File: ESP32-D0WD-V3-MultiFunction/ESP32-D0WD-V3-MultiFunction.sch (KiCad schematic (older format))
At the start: 0 parts

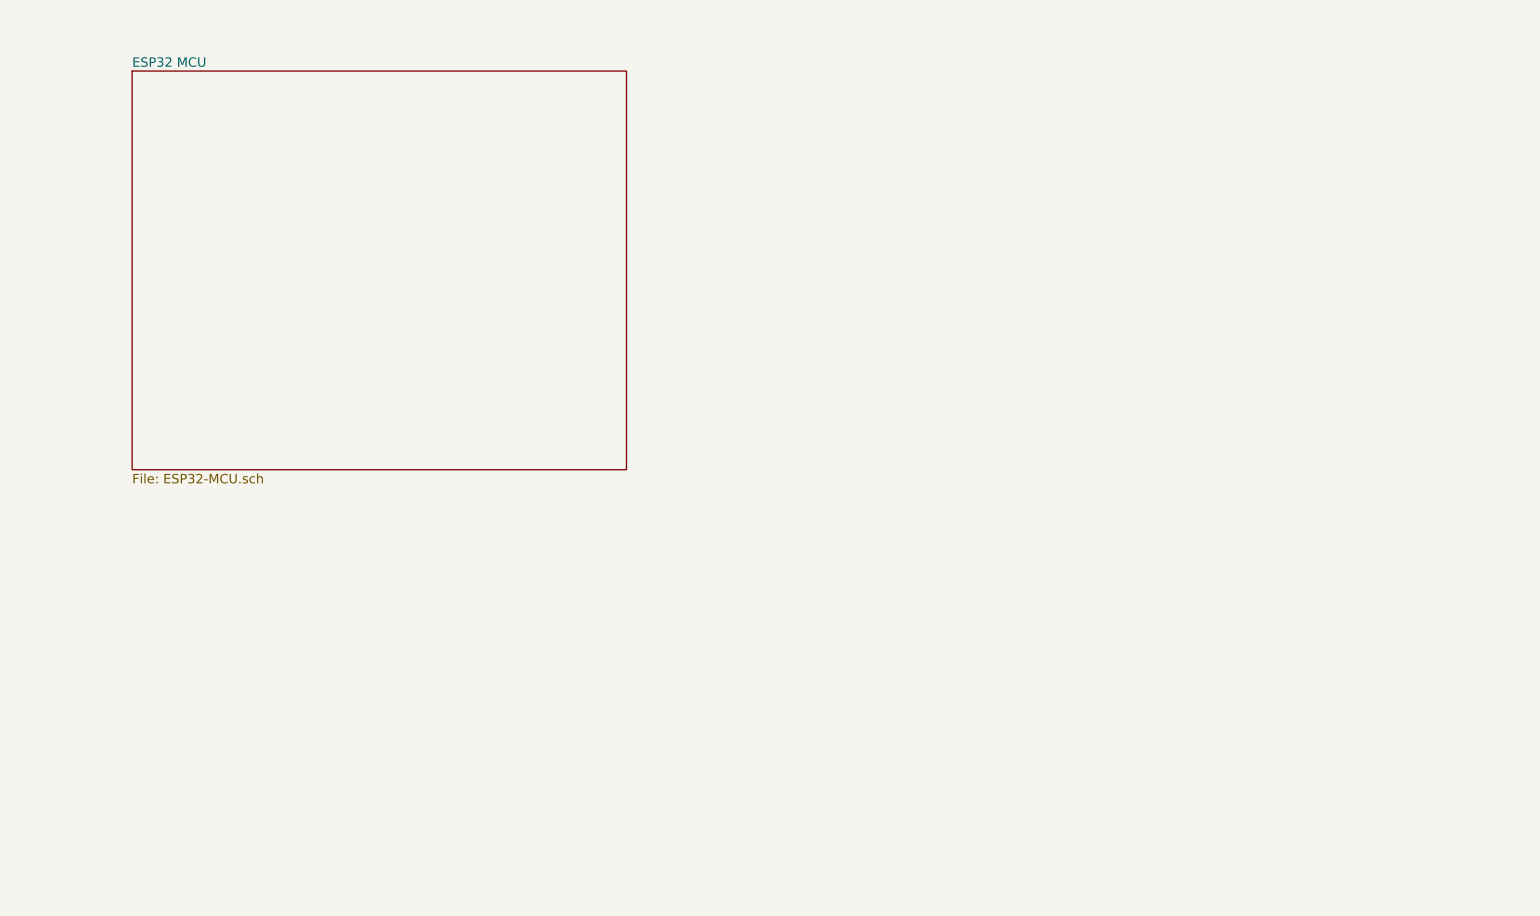
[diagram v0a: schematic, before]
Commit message: Initial draft of bare-chip ESP32 Multifunction board.
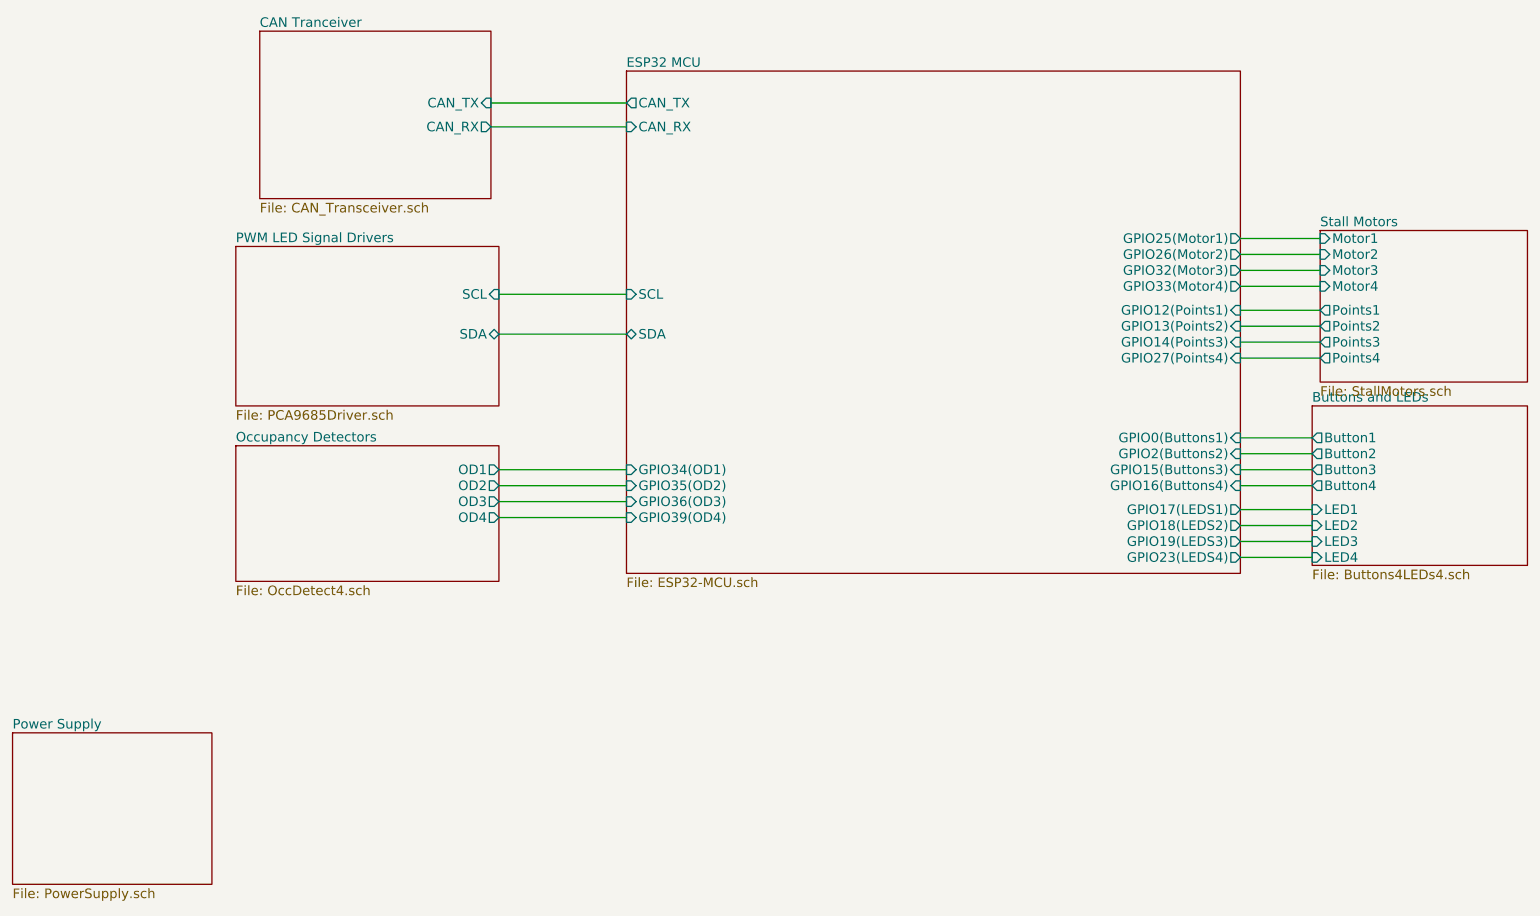
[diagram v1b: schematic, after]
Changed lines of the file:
@@
 LIBS:ESP32-D0WD-V3
 LIBS:W25Q32JVSSIQ
+LIBS:umh3n
+LIBS:lm2574n-5
+LIBS:tc442x
+LIBS:4814p-2
+LIBS:pca9685
+LIBS:tbd62x83a
+LIBS:sn65hvd233-ht
+LIBS:ESP32-D0WD-V3-MultiFunction-cache
 EELAYER 25 0
 EELAYER END
 $Descr A4 11693 8268
 encoding utf-8
-Sheet 1 2
+Sheet 1 8
 Title ""
 Date ""
@@
 $EndDescr
 $Sheet
-S 2050 1350 3100 2500
+S 5150 1350 3850 3150
 U 62ACDEF5
 F0 "ESP32 MCU" 59
 F1 "ESP32-MCU.sch" 59
+F2 "CAN_TX" O L 5150 1550 60
+F3 "CAN_RX" I L 5150 1700 60
+F4 "SCL" I L 5150 2750 60
+F5 "SDA" B L 5150 3000 60
+F6 "GPIO19(LEDS3)" O R 9000 4300 60
+F7 "GPIO23(LEDS4)" O R 9000 4400 60
+F8 "GPIO18(LEDS2)" O R 9000 4200 60
+F9 "GPIO17(LEDS1)" O R 9000 4100 60
+F10 "GPIO16(Buttons4)" I R 9000 3950 60
+F11 "GPIO0(Buttons1)" I R 9000 3650 60
+F12 "GPIO2(Buttons2)" I R 9000 3750 60
+F13 "GPIO27(Points4)" I R 9000 3150 60
+F14 "GPIO26(Motor2)" O R 9000 2500 60
+F15 "GPIO25(Motor1)" O R 9000 2400 60
+F16 "GPIO34(OD1)" I L 5150 3850 60
+F17 "GPIO35(OD2)" I L 5150 3950 60
+F18 "GPIO36(OD3)" I L 5150 4050 60
+F19 "GPIO39(OD4)" I L 5150 4150 60
+F20 "GPIO32(Motor3)" O R 9000 2600 60
+F21 "GPIO33(Motor4)" O R 9000 2700 60
+F22 "GPIO12(Points1)" I R 9000 2850 60
+F23 "GPIO13(Points2)" I R 9000 2950 60
+F24 "GPIO14(Points3)" I R 9000 3050 60
+F25 "GPIO15(Buttons3)" I R 9000 3850 60
 $EndSheet
+$Sheet
+S 1300 5500 1250 950
+U 62AF1057
+F0 "Power Supply" 60
+F1 "PowerSupply.sch" 60
+$EndSheet
+$Sheet
+S 9450 3450 1350 1000
+U 62AF1547
+F0 "Buttons and LEDs" 60
+F1 "Buttons4LEDs4.sch" 60
+F2 "LED1" I L 9450 4100 60
+F3 "LED2" I L 9450 4200 60
+F4 "LED3" I L 9450 4300 60
+F5 "LED4" I L 9450 4400 60
+F6 "Button1" O L 9450 3650 60
+F7 "Button2" O L 9450 3750 60
+F8 "Button3" O L 9450 3850 60
+F9 "Button4" O L 9450 3950 60
+$EndSheet
+$Sheet
+S 9500 2350 1300 950
+U 62AF637B
+F0 "Stall Motors" 60
+F1 "StallMotors.sch" 60
+F2 "Points1" O L 9500 2850 60
+F3 "Points2" O L 9500 2950 60
+F4 "Points3" O L 9500 3050 60
+F5 "Points4" O L 9500 3150 60
+F6 "Motor1" I L 9500 2400 60
+F7 "Motor2" I L 9500 2500 60
+F8 "Motor3" I L 9500 2600 60
+F9 "Motor4" I L 9500 2700 60
+$EndSheet
+$Sheet
+S 2700 3700 1650 850
+U 62AFE480
+F0 "Occupancy Detectors" 60
+F1 "OccDetect4.sch" 60
+F2 "OD1" O R 4350 3850 60
+F3 "OD2" O R 4350 3950 60
+F4 "OD3" O R 4350 4050 60
+F5 "OD4" O R 4350 4150 60
+$EndSheet
+$Sheet
+S 2700 2450 1650 1000
+U 62AFFF5E
+F0 "PWM LED Signal Drivers" 60
+F1 "PCA9685Driver.sch" 60
+F2 "SCL" I R 4350 2750 60
+F3 "SDA" B R 4350 3000 60
+$EndSheet
+Wire Wire Line
+	9000 4400 9450 4400
+Wire Wire Line
+	9000 4300 9450 4300
+Wire Wire Line
+	9000 4200 9450 4200
+Wire Wire Line
+	9000 4100 9450 4100
+Wire Wire Line
+	9000 3950 9450 3950
+Wire Wire Line
+	9000 3850 9450 3850
+Wire Wire Line
+	9000 3750 9450 3750
+Wire Wire Line
+	9000 3650 9450 3650
+Wire Wire Line
+	9000 2400 9500 2400
+Wire Wire Line
+	9000 2500 9500 2500
+Wire Wire Line
+	9000 2600 9500 2600
+Wire Wire Line
+	9000 2700 9500 2700
+Wire Wire Line
+	9000 2850 9500 2850
+Wire Wire Line
+	9000 2950 9500 2950
+Wire Wire Line
+	9000 3050 9500 3050
+Wire Wire Line
+	9000 3150 9500 3150
+Wire Wire Line
+	4350 3850 5150 3850
+Wire Wire Line
+	5150 3950 4350 3950
+Wire Wire Line
+	5150 4050 4350 4050
+Wire Wire Line
+	5150 4150 4350 4150
+Wire Wire Line
+	5150 2750 4350 2750
+Wire Wire Line
+	5150 3000 4350 3000
+$Sheet
+S 2850 1100 1450 1050
+U 62B03516
+F0 "CAN Tranceiver" 60
+F1 "CAN_Transceiver.sch" 60
+F2 "CAN_TX" I R 4300 1550 60
+F3 "CAN_RX" O R 4300 1700 60
+$EndSheet
+Wire Wire Line
+	5150 1550 4300 1550
+Wire Wire Line
+	5150 1700 4300 1700
 $EndSCHEMATC

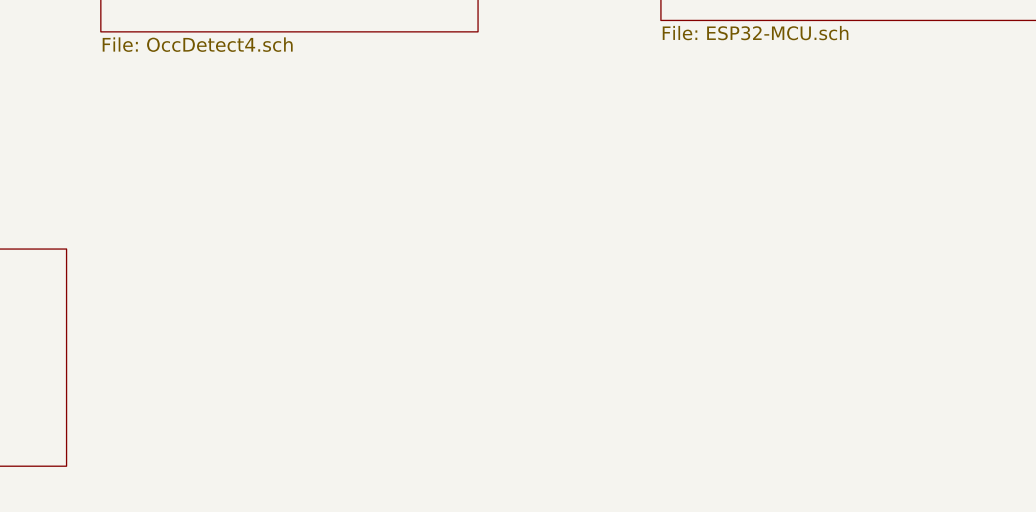
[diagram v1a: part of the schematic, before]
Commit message: All but the MPU on the ESP32-D0WD-V3-MultiFunction is done.
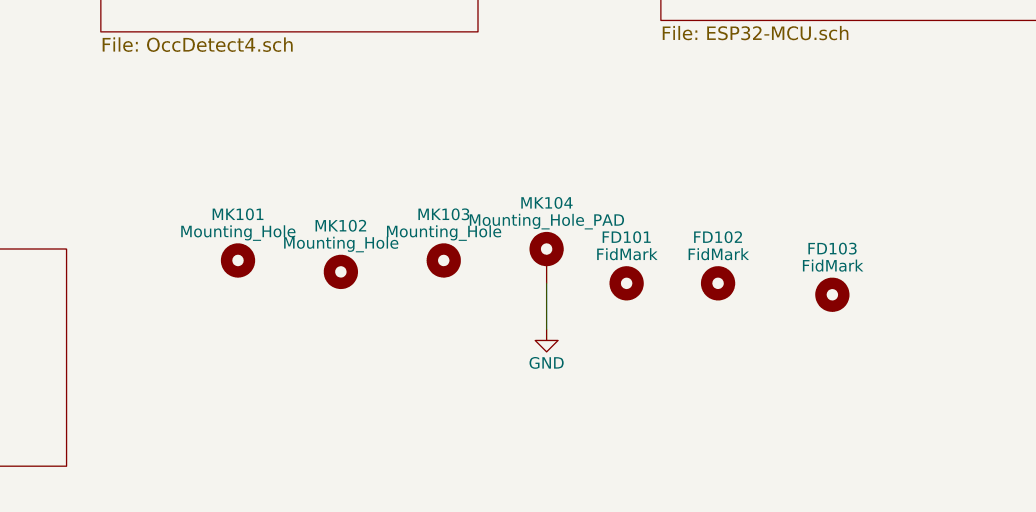
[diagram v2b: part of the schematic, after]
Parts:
- added FD101, FD102, FD103: FidMark, Fiducials:Fiducial_1mm_Dia_2.54mm_Outer_CopperTop, symbol Mounting_Hole
- added MK101, MK102, MK103: Mounting_Hole, Mounting_Holes:MountingHole_3.7mm, symbol Mounting_Hole
- added MK104: Mounting_Hole_PAD, Mounting_Holes:MountingHole_3.7mm_Pad, symbol Mounting_Hole_PAD
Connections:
- new net GND: MK104.1
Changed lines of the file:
@@
 EESchema Schematic File Version 2
+LIBS:ESP32-D0WD-V3-MultiFunction-rescue
 LIBS:power
 LIBS:device
@@
 LIBS:tbd62x83a
 LIBS:sn65hvd233-ht
+LIBS:mechanical
+LIBS:graphic_symbols
 LIBS:ESP32-D0WD-V3-MultiFunction-cache
 EELAYER 25 0
@@
 Wire Wire Line
 	5150 1700 4300 1700
+$Comp
+L Mounting_Hole MK101
+U 1 1 62AFDBC7
+P 3300 5550
+F 0 "MK101" H 3300 5750 50  0000 C CNN
+F 1 "Mounting_Hole" H 3300 5675 50  0000 C CNN
+F 2 "Mounting_Holes:MountingHole_3.7mm" H 3300 5550 50  0001 C CNN
+F 3 "" H 3300 5550 50  0001 C CNN
+	1    3300 5550
+	1    0    0    -1
+$EndComp
+$Comp
+L Mounting_Hole MK102
+U 1 1 62AFDD12
+P 3750 5600
+F 0 "MK102" H 3750 5800 50  0000 C CNN
+F 1 "Mounting_Hole" H 3750 5725 50  0000 C CNN
+F 2 "Mounting_Holes:MountingHole_3.7mm" H 3750 5600 50  0001 C CNN
+F 3 "" H 3750 5600 50  0001 C CNN
+	1    3750 5600
+	1    0    0    -1
+$EndComp
+$Comp
+L Mounting_Hole MK103
+U 1 1 62AFDE4B
+P 4200 5550
+F 0 "MK103" H 4200 5750 50  0000 C CNN
+F 1 "Mounting_Hole" H 4200 5675 50  0000 C CNN
+F 2 "Mounting_Holes:MountingHole_3.7mm" H 4200 5550 50  0001 C CNN
+F 3 "" H 4200 5550 50  0001 C CNN
+	1    4200 5550
+	1    0    0    -1
+$EndComp
+$Comp
+L Mounting_Hole_PAD MK104
+U 1 1 62AFDF86
+P 4650 5550
+F 0 "MK104" H 4650 5800 50  0000 C CNN
+F 1 "Mounting_Hole_PAD" H 4650 5725 50  0000 C CNN
+F 2 "Mounting_Holes:MountingHole_3.7mm_Pad" H 4650 5550 50  0001 C CNN
+F 3 "" H 4650 5550 50  0001 C CNN
+	1    4650 5550
+	1    0    0    -1
+$EndComp
+$Comp
+L GND #PWR01
+U 1 1 62AFE0C3
+P 4650 5850
+F 0 "#PWR01" H 4650 5600 50  0001 C CNN
+F 1 "GND" H 4650 5700 50  0000 C CNN
+F 2 "" H 4650 5850 50  0001 C CNN
+F 3 "" H 4650 5850 50  0001 C CNN
+	1    4650 5850
+	1    0    0    -1
+$EndComp
+Wire Wire Line
+	4650 5650 4650 5850
+$Comp
+L Mounting_Hole FD101
+U 1 1 62AFE875
+P 5000 5650
+F 0 "FD101" H 5000 5850 50  0000 C CNN
+F 1 "FidMark" H 5000 5775 50  0000 C CNN
+F 2 "Fiducials:Fiducial_1mm_Dia_2.54mm_Outer_CopperTop" H 5000 5650 50  0001 C CNN
+F 3 "" H 5000 5650 50  0001 C CNN
+	1    5000 5650
+	1    0    0    -1
+$EndComp
+$Comp
+L Mounting_Hole FD102
+U 1 1 62AFEAF8
+P 5400 5650
+F 0 "FD102" H 5400 5850 50  0000 C CNN
+F 1 "FidMark" H 5400 5775 50  0000 C CNN
+F 2 "Fiducials:Fiducial_1mm_Dia_2.54mm_Outer_CopperTop" H 5400 5650 50  0001 C CNN
+F 3 "" H 5400 5650 50  0001 C CNN
+	1    5400 5650
+	1    0    0    -1
+$EndComp
+$Comp
+L Mounting_Hole FD103
+U 1 1 62AFED78
+P 5900 5700
+F 0 "FD103" H 5900 5900 50  0000 C CNN
+F 1 "FidMark" H 5900 5825 50  0000 C CNN
+F 2 "Fiducials:Fiducial_1mm_Dia_2.54mm_Outer_CopperTop" H 5900 5700 50  0001 C CNN
+F 3 "" H 5900 5700 50  0001 C CNN
+	1    5900 5700
+	1    0    0    -1
+$EndComp
 $EndSCHEMATC
